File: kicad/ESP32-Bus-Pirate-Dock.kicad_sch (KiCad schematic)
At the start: 6 parts, among them J1 Conn_01x10, J2 Conn_01x20_MountingPin, J3 Conn_01x20_MountingPin, U1 ESP32-S3-DEVKITC-1-N8R2

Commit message: File title changes
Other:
- note removed: "ESP32-Bus-Pirate Dock"
- title: (none) -> ESP32 Bus Pirate Dock
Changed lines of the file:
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@@
 	(generator_version "9.0")
 	(paper "A4")
-	(text "ESP32-Bus-Pirate Dock"
-		(exclude_from_sim no)
-		(at 216.408 173.736 0)
-		(effects
-			(font
-				(size 3.81 3.81)
-				(thickness 0.762)
-				(bold yes)
-				(color 72 0 0 1)
-			)
-		)
+	(title_block
+		(title "ESP32 Bus Pirate Dock")
+		(date "2025-09-21")
 	)
 	(wire

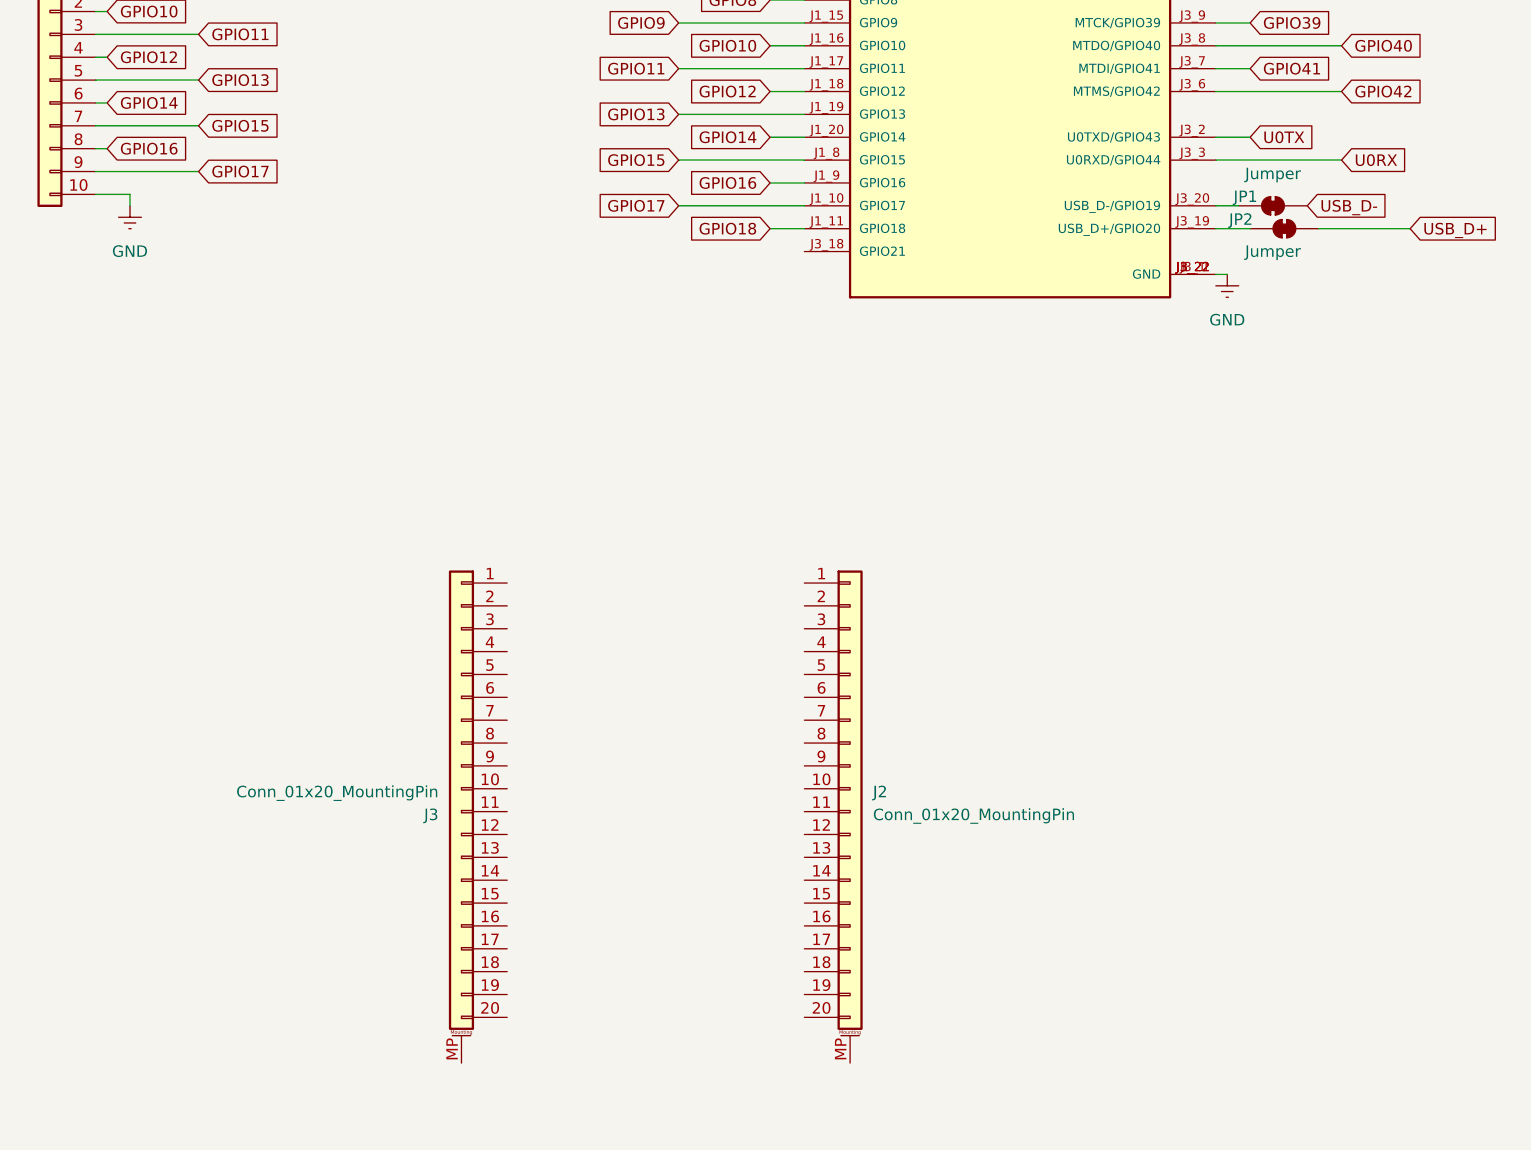
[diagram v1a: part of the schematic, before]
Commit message: Modified schematic and PCB
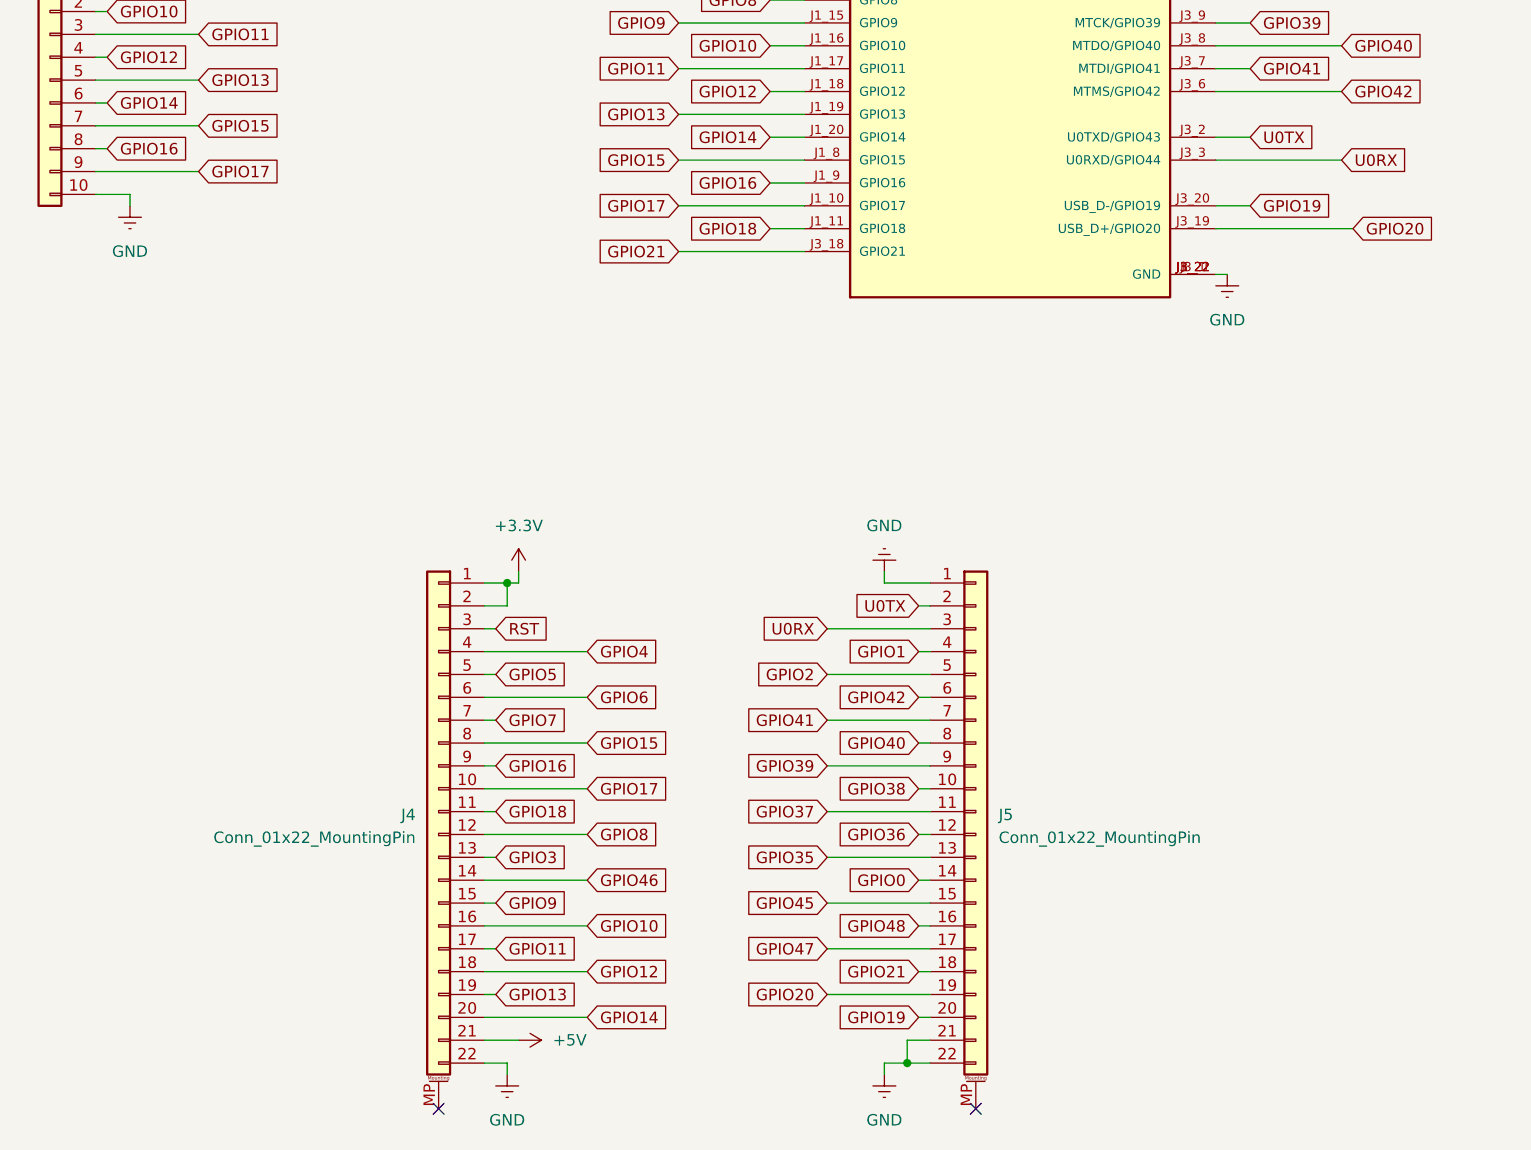
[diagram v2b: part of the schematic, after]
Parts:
- removed J2, J3: Conn_01x20_MountingPin, Connector_PinHeader_2.54mm:PinHeader_1x20_P2.54mm_Vertical, symbol Connector_Generic_MountingPin:Conn_01x20_MountingPin
- removed JP1, JP2: Jumper, Jumper:SolderJumper-2_P1.3mm_Bridged_Pad1.0x1.5mm, symbol Jumper:SolderJumper_2_Bridged
- added J4, J5: Conn_01x22_MountingPin, Connector_PinHeader_2.54mm:PinHeader_1x22_P2.54mm_Vertical, symbol Connector_Generic_MountingPin:Conn_01x22_MountingPin
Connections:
- net +3.3V: now also J4.1 (Pin_1), J4.2 (Pin_2)
- net +5V: now also J4.21 (Pin_21)
- net GND: now also J4.22 (Pin_22), J5.1 (Pin_1), J5.21 (Pin_21), J5.22 (Pin_22)
- net GPIO0: now also J5.14 (Pin_14)
- net GPIO1: now also J5.4 (Pin_4)
- net GPIO10: now also J4.16 (Pin_16)
- net GPIO11: now also J4.17 (Pin_17)
- net GPIO12: now also J4.18 (Pin_18)
- net GPIO13: now also J4.19 (Pin_19)
- net GPIO14: now also J4.20 (Pin_20)
- net GPIO15: now also J4.8 (Pin_8)
- net GPIO16: now also J4.9 (Pin_9)
- net GPIO17: now also J4.10 (Pin_10)
- net GPIO18: now also J4.11 (Pin_11)
- net GPIO2: now also J5.5 (Pin_5)
- net GPIO3: now also J4.13 (Pin_13)
- net GPIO35: now also J5.13 (Pin_13)
- net GPIO36: now also J5.12 (Pin_12)
- net GPIO37: now also J5.11 (Pin_11)
- net GPIO38: now also J5.10 (Pin_10)
- net GPIO39: now also J5.9 (Pin_9)
- net GPIO4: now also J4.4 (Pin_4)
- net GPIO40: now also J5.8 (Pin_8)
- net GPIO41: now also J5.7 (Pin_7)
- net GPIO42: now also J5.6 (Pin_6)
- net GPIO45: now also J5.15 (Pin_15)
- net GPIO46: now also J4.14 (Pin_14)
- net GPIO47: now also J5.17 (Pin_17)
- net GPIO48: now also J5.16 (Pin_16)
- net GPIO5: now also J4.5 (Pin_5)
- net GPIO6: now also J4.6 (Pin_6)
- net GPIO7: now also J4.7 (Pin_7)
- net GPIO8: now also J4.12 (Pin_12)
- net GPIO9: now also J4.15 (Pin_15)
- net RST: now also J4.3 (Pin_3)
- net U0RX: now also J5.3 (Pin_3)
- net U0TX: now also J5.2 (Pin_2)
- net GPIO21: now reaches U1.J3_18 (GPIO21)
- net GPIO21: now also J5.18 (Pin_18)
- net GPIO20: now reaches U1.J3_19 (USB_D+/GPIO20)
- net GPIO20: now also J5.19 (Pin_19)
- net GPIO19: now reaches U1.J3_20 (USB_D-/GPIO19)
- net GPIO19: now also J5.20 (Pin_20)
- no-connect marks 0 -> 2

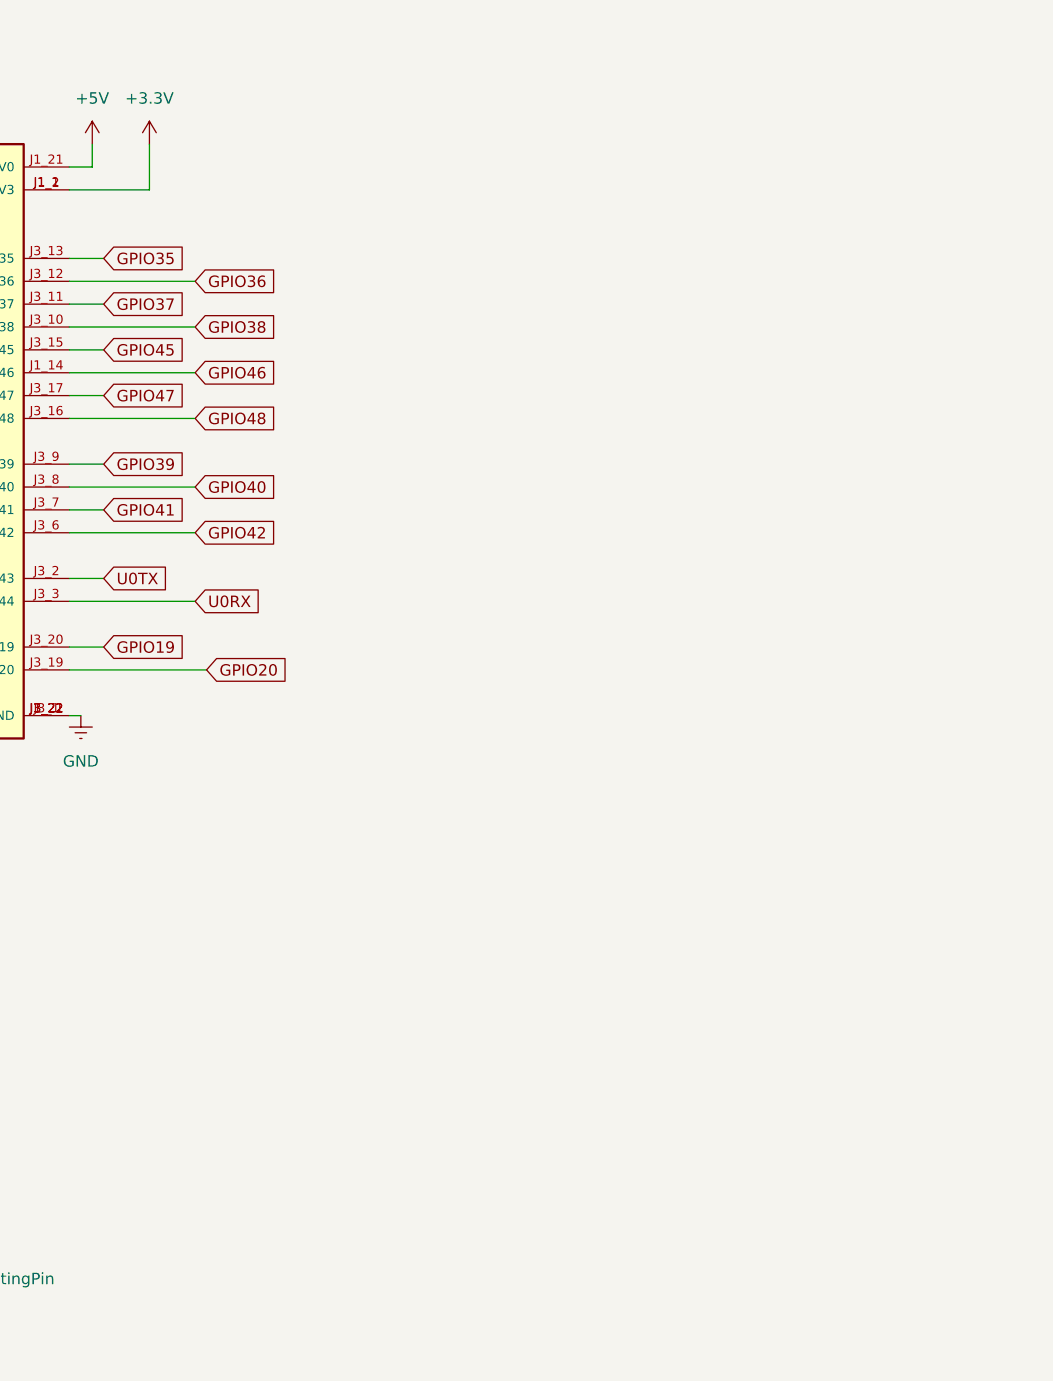
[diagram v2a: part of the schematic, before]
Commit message: Added 1.8V and another buttons
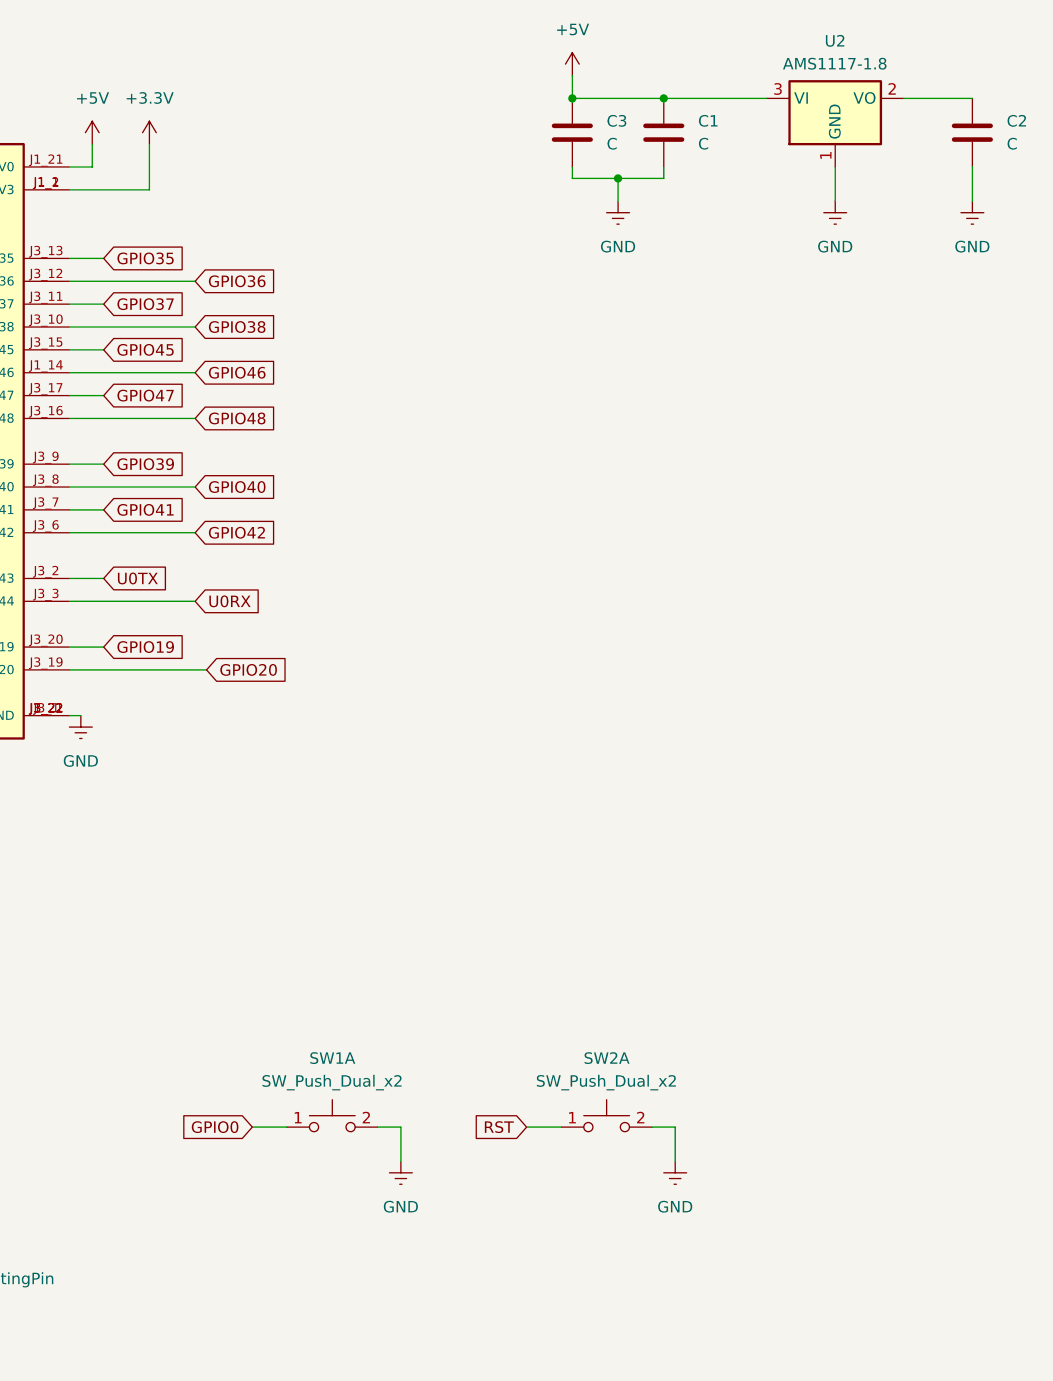
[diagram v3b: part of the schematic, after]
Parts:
- added C1, C2, C3: C, symbol Device:C
- added SW1, SW2: SW_Push_Dual_x2, symbol Switch:SW_Push_Dual_x2
- added U2: AMS1117-1.8, Package_TO_SOT_SMD:SOT-223-3_TabPin2, symbol Regulator_Linear:AMS1117-1.8
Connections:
- net +5V: now also C1.1, C3.1, U2.3 (VI)
- net GND: now also C1.2, C2.2, C3.2, SW1.2 (D), SW2.2 (D), U2.1 (GND)
- net GPIO0: now also SW1.1 (C)
- net RST: now also SW2.1 (C)
- new net: C2.1, U2.2 (VO)

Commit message: Wired more
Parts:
- added C4: 0.1u, Capacitor_SMD:C_0805_2012Metric, symbol Device:C
- C1, C2: value C -> 47u; footprint (none) -> Capacitor_SMD:C_0805_2012Metric
- C3: value C -> 0.1u; footprint (none) -> Capacitor_SMD:C_0805_2012Metric
- SW1: value SW_Push_Dual_x2 -> SW_BOOT
- SW2: value SW_Push_Dual_x2 -> SW_RST
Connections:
- net GND: now also C4.2
- net GPIO10: now also J1.6 (Pin_6); no longer J1.2 (Pin_2)
- net GPIO11: now also J1.7 (Pin_7); no longer J1.3 (Pin_3)
- net GPIO12: now also J1.8 (Pin_8); no longer J1.4 (Pin_4)
- net GPIO13: now also J1.9 (Pin_9); no longer J1.5 (Pin_5)
- net GPIO14: no longer J1.6 (Pin_6)
- net GPIO15: now also J1.2 (Pin_2); no longer J1.7 (Pin_7)
- net GPIO16: now also J1.3 (Pin_3); no longer J1.8 (Pin_8)
- net GPIO17: now also J1.4 (Pin_4); no longer J1.9 (Pin_9)
- net GPIO18: now also J1.5 (Pin_5)
- net +1V8: now reaches C2.1, U2.2 (VO)
- net +1V8: now also C4.1
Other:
- moved on the sheet: J4, J5, SW1A, SW2A
